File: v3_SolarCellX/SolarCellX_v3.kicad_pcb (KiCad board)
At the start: 6 copper layers, 48.4 x 48.4 mm, 13 parts, among them J1 symbols_XF2M-1015-1A

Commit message: Finished the Magnetorquer
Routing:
- net (no net): track 4237.9 -> 15951.6 mm

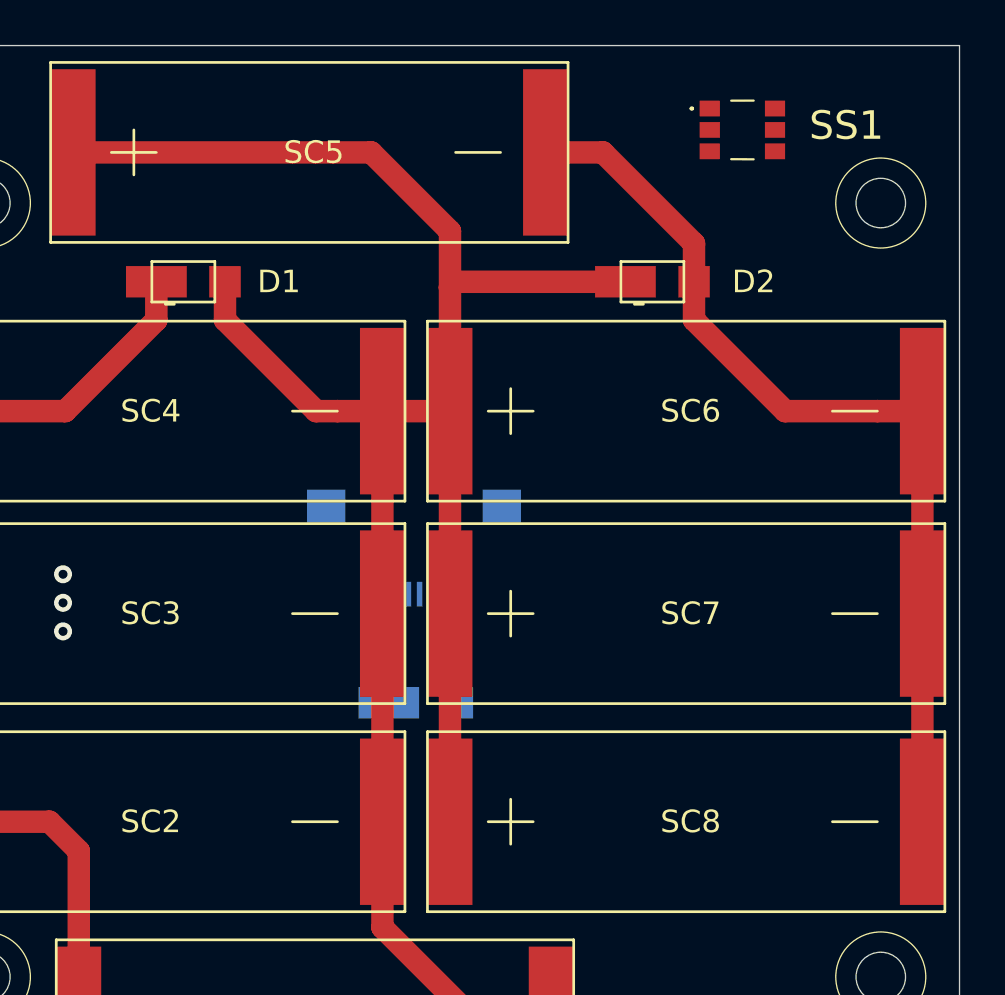
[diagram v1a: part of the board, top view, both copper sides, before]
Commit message: Cleaned up the Magnetorquer and added labels
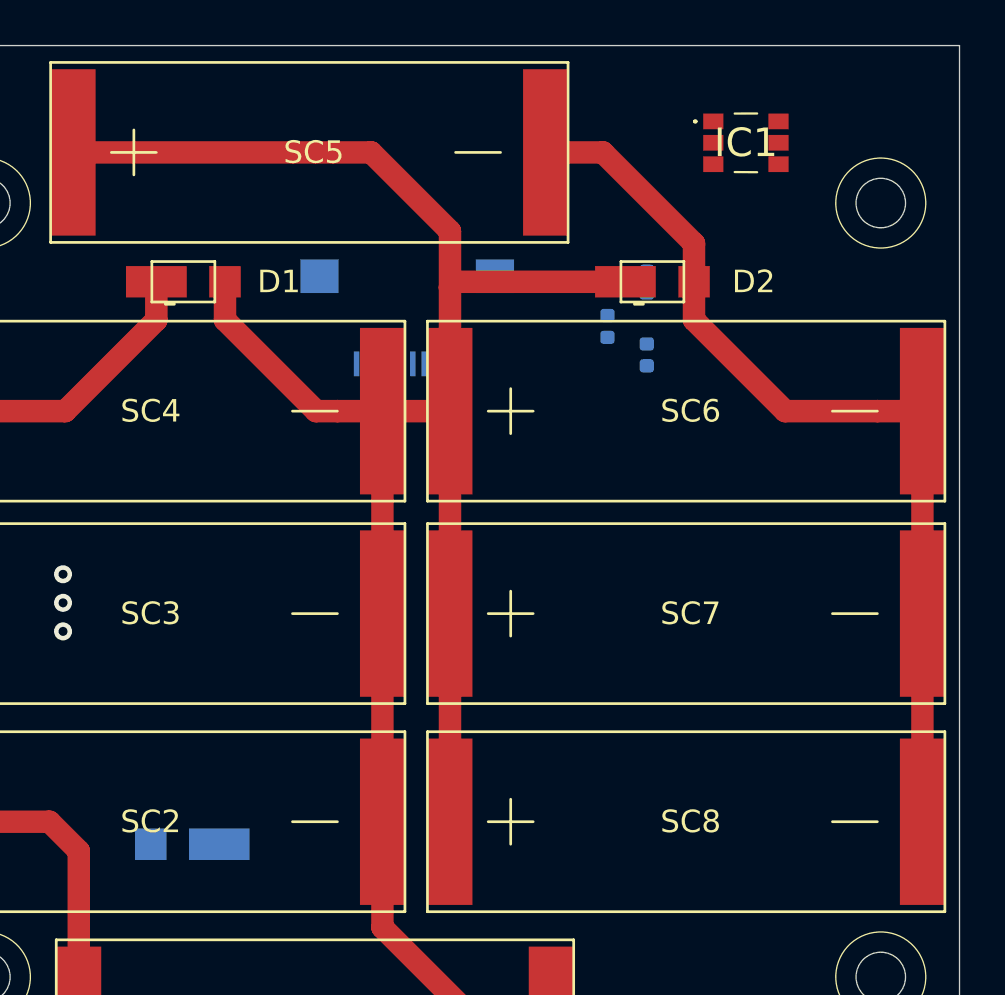
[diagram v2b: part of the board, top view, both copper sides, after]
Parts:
- removed SS1: symbols_TSL2561, misc-circuits:TSL2561
- added C5: 0.1uF, Capacitor_SMD:C_0402_1005Metric, B.Cu at (122.8, 52.5)
- added IC1: TSL2561, misc-circuits:TSL2561, F.Cu at (128.9, 44.3)
- added R12: 0, Resistor_SMD:R_0402_1005Metric, B.Cu at (124.5, 50.5)
- added R13: 0, Resistor_SMD:R_0402_1005Metric, B.Cu at (124.5, 53.8)
- J1: value symbols_XF2M-1015-1A -> XF2M-1015-1A
- moved D3 11.8 mm to (104.3, 75.5), turned to 180 degrees
- moved J1 10.2 mm to (113.8, 54.1)
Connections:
- net Net-(D3-Pad1) renamed VSolar
- net Net-(J1-Pad2) renamed BATT_P
- net Net-(J1-Pad4) renamed BATT_N
- net Net-(J1-Pad5) renamed BURN1
- net Net-(J1-Pad6) renamed COIL_P
- net Net-(J1-Pad8) renamed COIL_N
- D2 pad 2: Net-(D2-Pad2) -> GND
- J1 pad 1: Net-(J1-Pad1) -> SDA1
- J1 pad 10: Net-(J1-Pad10) -> GND
- J1 pad 3: Net-(J1-Pad3) -> SCL1
- J1 pad 7: Net-(J1-Pad7) -> +3V3
- J1 pad 9: Net-(J1-Pad9) -> GND
- SC5 pad 2: Net-(D2-Pad2) -> GND
- SC6 pad 2: Net-(D2-Pad2) -> GND
- SC7 pad 2: Net-(D2-Pad2) -> GND
- SC8 pad 2: Net-(D2-Pad2) -> GND
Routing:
- net (no net): track 15951.6 -> 16333.0 mm
- net Net-(D2-Pad2): track 41.8 -> 0.00 mm
- net GND: track 0.00 -> 41.8 mm
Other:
- board text added: "Coil +"
- board text added: "Coil -"

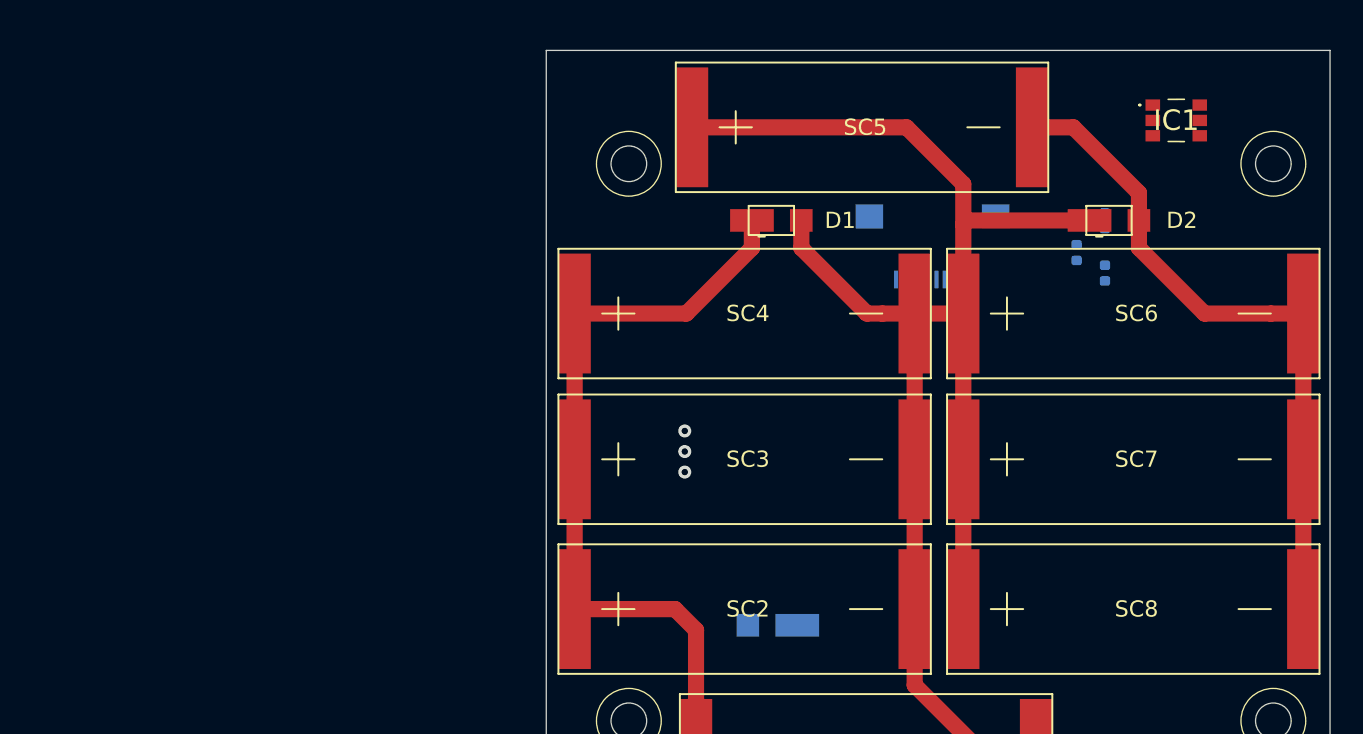
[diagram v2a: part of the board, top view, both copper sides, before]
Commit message: making libraries locally referenced for easy import
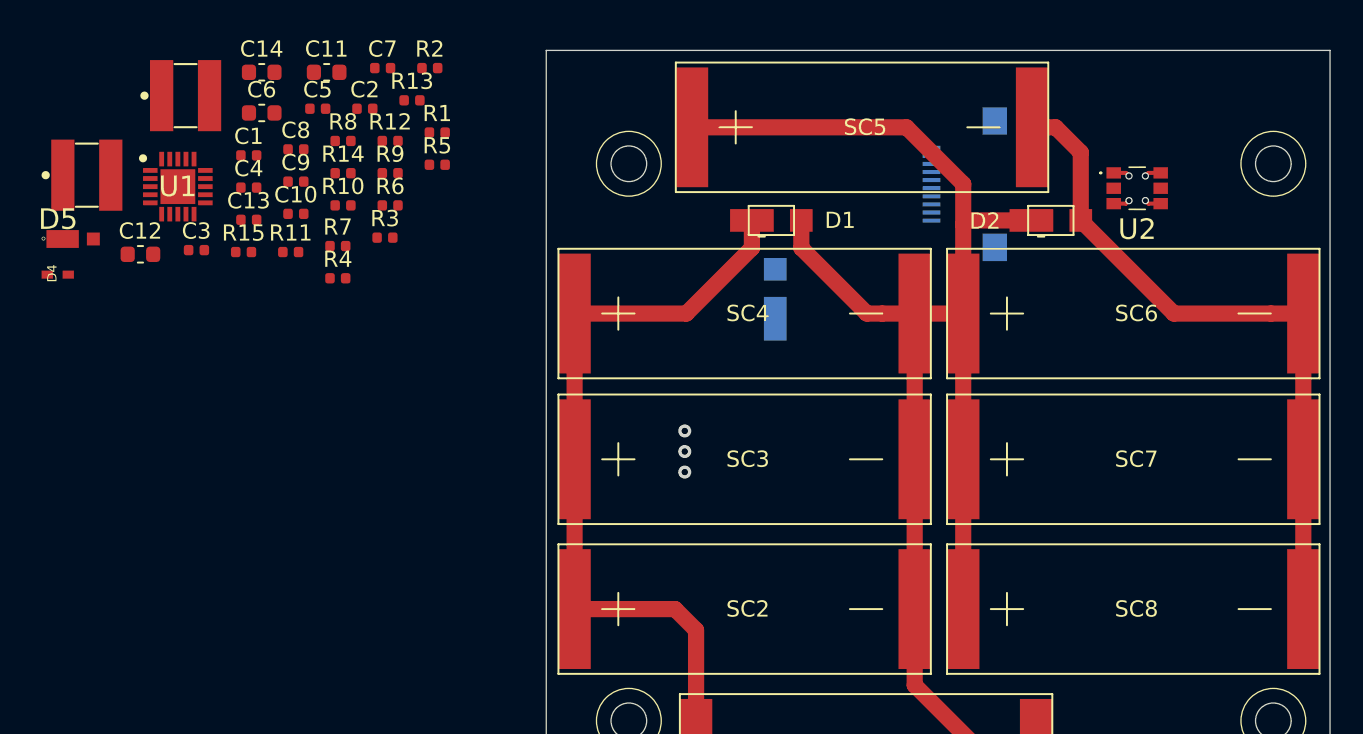
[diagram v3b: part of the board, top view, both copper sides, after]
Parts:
- removed IC1: TSL2561, misc-circuits:TSL2561
- added C1: 0.1uF, Capacitor_SMD:C_0402_1005Metric, F.Cu at (71.6, 46.5)
- added C10: 0.1uF, Capacitor_SMD:C_0402_1005Metric, F.Cu at (74.5, 50.1)
- added C11: 100uF, Capacitor_SMD:C_0603_1608Metric, F.Cu at (76.4, 41.4)
- added C12: 100uF, Capacitor_SMD:C_0603_1608Metric, F.Cu at (64.9, 52.6)
- added C13: 0.1uF, Capacitor_SMD:C_0402_1005Metric, F.Cu at (71.6, 50.5)
- added C14: 100uF, Capacitor_SMD:C_0603_1608Metric, F.Cu at (72.4, 41.4)
- added C2: 1.0uF, Capacitor_SMD:C_0402_1005Metric, F.Cu at (78.8, 43.6)
- added C3: 0.1uF, Capacitor_SMD:C_0402_1005Metric, F.Cu at (68.4, 52.3)
- added C4: 4.7uF, Capacitor_SMD:C_0402_1005Metric, F.Cu at (71.6, 48.5)
- added C6: 100uF, Capacitor_SMD:C_0603_1608Metric, F.Cu at (72.4, 43.9)
- added C7: 22uF, Capacitor_SMD:C_0402_1005Metric, F.Cu at (79.9, 41.1)
- added C8: 4.7uF, Capacitor_SMD:C_0402_1005Metric, F.Cu at (74.5, 46.1)
- added C9: 0.1uF, Capacitor_SMD:C_0402_1005Metric, F.Cu at (74.5, 48.1)
- added D4: SDM20U40-7, misc-circuits:SOD523, F.Cu at (59.8, 53.8)
- added D5: MSS1P4-M3_89A, custom-footprints:MICROSMP, F.Cu at (60.8, 51.6)
- added L1: 22uH-LPS4018-223MR, misc-circuits:LPS4018, F.Cu at (67.7, 42.8)
- added L2: 10uH-LPS4018-103MR, misc-circuits:LPS4018, F.Cu at (61.6, 47.7)
- added R1: 0, Resistor_SMD:R_0402_1005Metric, F.Cu at (83.3, 45.1)
- added R10: 4.75M, Resistor_SMD:R_0402_1005Metric, F.Cu at (77.4, 49.6)
- added R11: 0, Resistor_SMD:R_0402_1005Metric, F.Cu at (74.2, 52.5)
- added R14: 0, Resistor_SMD:R_0402_1005Metric, F.Cu at (77.4, 47.6)
- added R15: 0, Resistor_SMD:R_0402_1005Metric, F.Cu at (71.3, 52.5)
- added R2: 0, Resistor_SMD:R_0402_1005Metric, F.Cu at (82.8, 41.1)
- added R3: 0, Resistor_SMD:R_0402_1005Metric, F.Cu at (80.0, 51.6)
- added R4: 7.32M, Resistor_SMD:R_0402_1005Metric, F.Cu at (77.1, 54.1)
- added R5: 5.62M, Resistor_SMD:R_0402_1005Metric, F.Cu at (83.3, 47.1)
- added R6: 374K, Resistor_SMD:R_0402_1005Metric, F.Cu at (80.4, 49.6)
- added R7: 8.25M, Resistor_SMD:R_0402_1005Metric, F.Cu at (77.1, 52.1)
- added R8: 4.53M, Resistor_SMD:R_0402_1005Metric, F.Cu at (77.4, 45.6)
- added R9: 8.25M, Resistor_SMD:R_0402_1005Metric, F.Cu at (80.4, 47.6)
- added U1: Value, misc-circuits:QFN50P350X350X100-21N-D, F.Cu at (67.2, 48.4)
- added U2: TSL2561, misc-circuits:TSL2561, F.Cu at (126.5, 48.5)
- C5: value 0.1uF -> 10nF; moved to F.Cu
- R12, R13: moved to F.Cu
- moved C5 47.7 mm to (75.9, 43.6), turned to 0 degrees
- moved R12 44.4 mm to (80.4, 45.6), turned to 0 degrees
- moved R13 44.1 mm to (81.7, 43.1), turned to 0 degrees
- moved D3 20.1 mm to (104.1, 55.4), turned to 90 degrees
- moved J1 5.89 mm to (113.8, 48.3), turned to 270 degrees
- moved D2 3.59 mm to (121.2, 50.5)
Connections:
- C5 pad 1: GND -> Net-(C5-Pad1)
- C5 pad 2: +3V3 -> GND
- R12 pad 1: Net-(IC1-Pad2) -> GND
- R12 pad 2: +3V3 -> Net-(R11-Pad1)
- R13 pad 1: GND -> Net-(C11-Pad1)
- R13 pad 2: Net-(IC1-Pad2) -> Net-(R11-Pad1)
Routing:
- net Net-(D1-Pad2): track 98.1 -> 94.7 mm
- net GND: track 41.8 -> 43.2 mm, vias 0 -> 1
- net +3V3: track 0.00 -> 1.02 mm, vias 0 -> 1
- net SDA1: track 0.00 -> 1.02 mm, vias 0 -> 1
- net SCL1: track 0.00 -> 1.02 mm, vias 0 -> 1
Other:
- net class Default: clearance 0.2 -> 0.127; trace_width 0.25 -> 0.249936; via_dia 0.8 -> 0.45; via_drill 0.4 -> 0.3
- rule pad_to_mask_clearance: 0.051 -> 0.0508
- rule trace_clearance: 0.2 -> 0.127
- rule via_min_size: 0.4 -> 0.45

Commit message: preparing to import misc-circuits
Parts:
- moved D3 14.2 mm to (100.3, 69.1), turned to 270 degrees
- moved J1 1.55 mm to (113.5, 46.7)
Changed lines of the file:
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@@
   (general
     (thickness 1.6)
-    (drawings 15)
+    (drawings 18)
     (tracks 1065)
     (zones 0)
@@
   )
   (module misc-circuits:XF2M-1015-1A (layer B.Cu)
-    (at 113.792 48.26 270)
+    (at 113.538 46.736 270)
     (descr XF2M-1015-1A)
     (tags Connector)
@@
   )
   (module "SolarCellParts:SB Diode" (layer B.Cu)
-    (at 104.14 55.372 90)
+    (at 100.33 69.088 270)
     (fp_text reference D3 (at 0.5 -2 90) (layer B.SilkS)
       (effects (font (size 1 1) (thickness 0.15)) (justify mirror))
@@
     (fp_line (start 1.4 -0.9) (end -1.4 -0.9) (layer B.SilkS) (width 0.12))
     (fp_line (start 1.4 0.9) (end 1.4 -0.9) (layer B.SilkS) (width 0.12))
-    (pad 2 smd rect (at 1.85 0 90) (size 1.4 1.4) (layers B.Cu B.Paste B.Mask)
+    (pad 2 smd rect (at 1.85 0 270) (size 1.4 1.4) (layers B.Cu B.Paste B.Mask)
       (net 2 "Net-(D1-Pad1)"))
-    (pad 1 smd rect (at -1.2 0 90) (size 2.7 1.4) (layers B.Cu B.Paste B.Mask)
+    (pad 1 smd rect (at -1.2 0 270) (size 2.7 1.4) (layers B.Cu B.Paste B.Mask)
       (net 5 VSolar))
   )
@@
       (net 2 "Net-(D1-Pad1)"))
   )
-  (gr_line (start 89.8906 60.005) (end 138.4046 60.005) (layer Dwgs.User) (width 0.05))
+  (gr_line (start 90.00236 41.605) (end 138.4046 41.605) (layer Dwgs.User) (width 0.05))
+  (gr_line (start 98.60236 39.939) (end 98.60236 60.005) (layer Dwgs.User) (width 0.05))
+  (gr_line (start 129.8046 39.939) (end 129.8046 60.005) (layer Dwgs.User) (width 0.05))
+  (gr_line (start 90.00236 60.005) (end 138.4046 60.005) (layer Dwgs.User) (width 0.05))
   (gr_text "Coil -" (at 101.854 66.04) (layer B.SilkS)
     (effects (font (size 1 1) (thickness 0.15)) (justify mirror))
